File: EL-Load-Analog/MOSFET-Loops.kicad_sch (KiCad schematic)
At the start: 102 parts, among them J2 SWEB8094AU-SW, J5 SWEB8094AU-RT, J7 Conn_01x02_Socket, Q201 2N7002, Q202 2N7002, Q203 IRFP250M, Q204 IRFP250M, Q205 2N7002, Q206 2N7002, Q207 IRFP250M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

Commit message: Working on #4,#2 fixed #8,#22
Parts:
- C213, C214, C227, C228: value 470p -> 1n; Part Name C_470.0pF_0805_20% -> C_1.0nF_0805_20%
- R203, R205, R223, R225: value 100k -> 22k; Part Name R_100.0kΩ_0805_1% -> R_22.0kΩ_0805_1%
- R221, R222: value 10k -> 0; Part Name R_10.0kΩ_0805_1% -> R_0.0Ω_0805_1%
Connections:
- net GND: no longer R211.2, R213.2, R231.2, R233.2
- new net GCOM: R211.2, R213.2, R231.2, R233.2
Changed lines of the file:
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@@
     )
   )
+  (global_label "GCOM" (shape input) (at 201.93 135.89 180) (fields_autoplaced)
+    (effects (font (size 1.27 1.27)) (justify right))
+    (property "Intersheetrefs" "${INTERSHEET_REFS}" (at 193.7023 135.89 0)
+      (effects (font (size 1.27 1.27)) (justify right) hide)
+    )
+  )
   (global_label "LoadPlus" (shape input) (at 132.08 92.71 0) (fields_autoplaced)
     (effects (font (size 1.27 1.27)) (justify left))
@@
     )
   )
+  (global_label "GCOM" (shape input) (at 66.04 60.96 180) (fields_autoplaced)
+    (effects (font (size 1.27 1.27)) (justify right))
+    (property "Intersheetrefs" "${INTERSHEET_REFS}" (at 57.8123 60.96 0)
+      (effects (font (size 1.27 1.27)) (justify right) hide)
+    )
+  )
   (global_label "LoadPlus" (shape input) (at 267.97 17.78 0) (fields_autoplaced)
     (effects (font (size 1.27 1.27)) (justify left))
@@
     )
   )
+  (global_label "GCOM" (shape input) (at 66.04 135.89 180) (fields_autoplaced)
+    (effects (font (size 1.27 1.27)) (justify right))
+    (property "Intersheetrefs" "${INTERSHEET_REFS}" (at 57.8123 135.89 0)
+      (effects (font (size 1.27 1.27)) (justify right) hide)
+    )
+  )
   (global_label "LoadPlus" (shape input) (at 132.08 17.78 0) (fields_autoplaced)
     (effects (font (size 1.27 1.27)) (justify left))
@@
     )
   )
+  (global_label "GCOM" (shape input) (at 201.93 60.96 180) (fields_autoplaced)
+    (effects (font (size 1.27 1.27)) (justify right))
+    (property "Intersheetrefs" "${INTERSHEET_REFS}" (at 193.7023 60.96 0)
+      (effects (font (size 1.27 1.27)) (justify right) hide)
+    )
+  )
   (global_label "LoadPlus" (shape output) (at 92.71 179.07 0) (fields_autoplaced)
     (effects (font (size 1.27 1.27)) (justify left))
@@
     )
   )
-  (symbol (lib_id "power:GND") (at 66.04 135.89 0) (unit 1)
-    (in_bom yes) (on_board yes) (dnp no) (fields_autoplaced)
-    (property "Reference" "#PWR0218" (at 66.04 142.24 0)
-      (effects (font (size 1.27 1.27)) hide)
-    )
-    (property "Value" "GND" (at 66.04 140.97 0)
-      (effects (font (size 1.27 1.27)) hide)
-    )
-    (property "Footprint" "" (at 66.04 135.89 0)
-      (effects (font (size 1.27 1.27)) hide)
-    )
-    (property "Datasheet" "" (at 66.04 135.89 0)
-      (effects (font (size 1.27 1.27)) hide)
-    )
-    (pin "1")
-    (instances
-      (project "EL-Load-Analog"
-        (path "/51d9228f-95b8-4f0d-bdba-83c3975c517c/8af1df1b-1025-4aef-94e0-10ff3284a07d"
-          (reference "#PWR0218") (unit 1)
-        )
-      )
-    )
-  )
   (symbol (lib_id "Amplifier_Operational:LM318H") (at 185.42 29.21 0) (unit 1)
     (in_bom yes) (on_board yes) (dnp no) (fields_autoplaced)
@@
       (effects (font (size 1.27 1.27)))
     )
-    (property "Value" "470p" (at 191.7763 116.84 90)
+    (property "Value" "1n" (at 191.7763 116.84 90)
       (effects (font (size 1.27 1.27)))
     )
@@
       (effects (font (size 1.27 1.27)) hide)
     )
-    (property "Part Name" "C_470.0pF_0805_20%" (at 191.77 120.65 0)
+    (property "Part Name" "C_1.0nF_0805_20%" (at 191.77 120.65 0)
       (effects (font (size 1.27 1.27)) hide)
     )
@@
       (effects (font (size 1.27 1.27)))
     )
-    (property "Value" "470p" (at 55.8863 116.84 90)
+    (property "Value" "1n" (at 55.8863 116.84 90)
       (effects (font (size 1.27 1.27)))
     )
@@
       (effects (font (size 1.27 1.27)) hide)
     )
-    (property "Part Name" "C_470.0pF_0805_20%" (at 55.88 120.65 0)
+    (property "Part Name" "C_1.0nF_0805_20%" (at 55.88 120.65 0)
       (effects (font (size 1.27 1.27)) hide)
     )
@@
       (effects (font (size 1.27 1.27)))
     )
-    (property "Value" "470p" (at 55.8863 41.91 90)
+    (property "Value" "1n" (at 55.8863 41.91 90)
       (effects (font (size 1.27 1.27)))
     )
@@
       (effects (font (size 1.27 1.27)) hide)
     )
-    (property "Part Name" "C_470.0pF_0805_20%" (at 55.88 45.72 0)
+    (property "Part Name" "C_1.0nF_0805_20%" (at 55.88 45.72 0)
       (effects (font (size 1.27 1.27)) hide)
     )
@@
       (effects (font (size 1.27 1.27)))
     )
-    (property "Value" "100k" (at 175.26 138.43 90)
+    (property "Value" "22k" (at 175.26 138.43 90)
       (effects (font (size 1.27 1.27)))
     )
@@
       (effects (font (size 1.27 1.27)) hide)
     )
-    (property "Part Name" "R_100.0kΩ_0805_1%" (at 172.72 138.43 0)
+    (property "Part Name" "R_22.0kΩ_0805_1%" (at 172.72 138.43 0)
       (effects (font (size 1.27 1.27)) hide)
     )
@@
       (effects (font (size 1.27 1.27)))
     )
-    (property "Value" "100k" (at 39.37 63.5 90)
+    (property "Value" "22k" (at 39.37 63.5 90)
       (effects (font (size 1.27 1.27)))
     )
@@
       (effects (font (size 1.27 1.27)) hide)
     )
-    (property "Part Name" "R_100.0kΩ_0805_1%" (at 36.83 63.5 0)
+    (property "Part Name" "R_22.0kΩ_0805_1%" (at 36.83 63.5 0)
       (effects (font (size 1.27 1.27)) hide)
     )
@@
       (effects (font (size 1.27 1.27)))
     )
-    (property "Value" "100k" (at 39.37 138.43 90)
+    (property "Value" "22k" (at 39.37 138.43 90)
       (effects (font (size 1.27 1.27)))
     )
@@
       (effects (font (size 1.27 1.27)) hide)
     )
-    (property "Part Name" "R_100.0kΩ_0805_1%" (at 36.83 138.43 0)
+    (property "Part Name" "R_22.0kΩ_0805_1%" (at 36.83 138.43 0)
       (effects (font (size 1.27 1.27)) hide)
     )
@@
     )
   )
-  (symbol (lib_id "power:GND") (at 66.04 60.96 0) (unit 1)
-    (in_bom yes) (on_board yes) (dnp no) (fields_autoplaced)
-    (property "Reference" "#PWR0217" (at 66.04 67.31 0)
-      (effects (font (size 1.27 1.27)) hide)
-    )
-    (property "Value" "GND" (at 66.04 66.04 0)
-      (effects (font (size 1.27 1.27)) hide)
-    )
-    (property "Footprint" "" (at 66.04 60.96 0)
-      (effects (font (size 1.27 1.27)) hide)
-    )
-    (property "Datasheet" "" (at 66.04 60.96 0)
-      (effects (font (size 1.27 1.27)) hide)
-    )
-    (pin "1")
-    (instances
-      (project "EL-Load-Analog"
-        (path "/51d9228f-95b8-4f0d-bdba-83c3975c517c/8af1df1b-1025-4aef-94e0-10ff3284a07d"
-          (reference "#PWR0217") (unit 1)
-        )
-      )
-    )
-  )
   (symbol (lib_id "power:-5V") (at 182.88 36.83 180) (unit 1)
     (in_bom yes) (on_board yes) (dnp no)
@@
       (effects (font (size 1.27 1.27)))
     )
-    (property "Value" "10k" (at 162.56 99.06 90)
+    (property "Value" "0" (at 162.56 99.06 90)
       (effects (font (size 1.27 1.27)))
     )
@@
       (effects (font (size 1.27 1.27)) hide)
     )
-    (property "Part Name" "R_10.0kΩ_0805_1%" (at 162.56 101.6 0)
+    (property "Part Name" "R_0.0Ω_0805_1%" (at 162.56 101.6 0)
       (effects (font (size 1.27 1.27)) hide)
     )
@@
     )
   )
-  (symbol (lib_id "power:GND") (at 201.93 135.89 0) (unit 1)
-    (in_bom yes) (on_board yes) (dnp no) (fields_autoplaced)
-    (property "Reference" "#PWR0245" (at 201.93 142.24 0)
-      (effects (font (size 1.27 1.27)) hide)
-    )
-    (property "Value" "GND" (at 201.93 140.97 0)
-      (effects (font (size 1.27 1.27)) hide)
-    )
-    (property "Footprint" "" (at 201.93 135.89 0)
-      (effects (font (size 1.27 1.27)) hide)
-    )
-    (property "Datasheet" "" (at 201.93 135.89 0)
-      (effects (font (size 1.27 1.27)) hide)
-    )
-    (pin "1")
-    (instances
-      (project "EL-Load-Analog"
-        (path "/51d9228f-95b8-4f0d-bdba-83c3975c517c/8af1df1b-1025-4aef-94e0-10ff3284a07d"
-          (reference "#PWR0245") (unit 1)
-        )
-      )
-    )
-  )
   (symbol (lib_id "Device:R") (at 267.97 72.39 0) (unit 1)
     (in_bom yes) (on_board yes) (dnp no) (fields_autoplaced)
@@
     )
   )
-  (symbol (lib_id "power:GND") (at 201.93 60.96 0) (unit 1)
-    (in_bom yes) (on_board yes) (dnp no) (fields_autoplaced)
-    (property "Reference" "#PWR0244" (at 201.93 67.31 0)
-      (effects (font (size 1.27 1.27)) hide)
-    )
-    (property "Value" "GND" (at 201.93 66.04 0)
-      (effects (font (size 1.27 1.27)) hide)
-    )
-    (property "Footprint" "" (at 201.93 60.96 0)
-      (effects (font (size 1.27 1.27)) hide)
-    )
-    (property "Datasheet" "" (at 201.93 60.96 0)
-      (effects (font (size 1.27 1.27)) hide)
-    )
-    (pin "1")
-    (instances
-      (project "EL-Load-Analog"
-        (path "/51d9228f-95b8-4f0d-bdba-83c3975c517c/8af1df1b-1025-4aef-94e0-10ff3284a07d"
-          (reference "#PWR0244") (unit 1)
-        )
-      )
-    )
-  )
   (symbol (lib_id "Device:R_Small") (at 204.47 29.21 90) (unit 1)
     (in_bom yes) (on_board yes) (dnp no)
@@
       (effects (font (size 1.27 1.27)))
     )
-    (property "Value" "10k" (at 162.56 24.13 90)
+    (property "Value" "0" (at 162.56 24.13 90)
       (effects (font (size 1.27 1.27)))
     )
@@
       (effects (font (size 1.27 1.27)) hide)
     )
-    (property "Part Name" "R_10.0kΩ_0805_1%" (at 162.56 26.67 0)
+    (property "Part Name" "R_0.0Ω_0805_1%" (at 162.56 26.67 0)
       (effects (font (size 1.27 1.27)) hide)
     )
@@
       (effects (font (size 1.27 1.27)))
     )
-    (property "Value" "100k" (at 175.26 63.5 90)
+    (property "Value" "22k" (at 175.26 63.5 90)
       (effects (font (size 1.27 1.27)))
     )
@@
       (effects (font (size 1.27 1.27)) hide)
     )
-    (property "Part Name" "R_100.0kΩ_0805_1%" (at 172.72 63.5 0)
+    (property "Part Name" "R_22.0kΩ_0805_1%" (at 172.72 63.5 0)
       (effects (font (size 1.27 1.27)) hide)
     )
@@
       (effects (font (size 1.27 1.27)))
     )
-    (property "Value" "470p" (at 191.7763 41.91 90)
+    (property "Value" "1n" (at 191.7763 41.91 90)
       (effects (font (size 1.27 1.27)))
     )
@@
       (effects (font (size 1.27 1.27)) hide)
     )
-    (property "Part Name" "C_470.0pF_0805_20%" (at 191.77 45.72 0)
+    (property "Part Name" "C_1.0nF_0805_20%" (at 191.77 45.72 0)
       (effects (font (size 1.27 1.27)) hide)
     )

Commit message: Added heatsink moutingholes, reverse polarity, moved snubbers.
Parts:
- added Q7: AOSP66923, Package_SO:SO-8_3.9x4.9mm_P1.27mm, symbol EL-Load:AOSP66923
- added R25: 0, Resistor_SMD:R_0805_2012Metric, symbol Device:R_Small
- added TP4: Imon3, TestPoint:TestPoint_Pad_1.0x1.0mm, symbol Connector:TestPoint_Flag
- added TP5: Imon1, TestPoint:TestPoint_Pad_1.0x1.0mm, symbol Connector:TestPoint_Flag
- added TP6: Imon4, TestPoint:TestPoint_Pad_1.0x1.0mm, symbol Connector:TestPoint_Flag
- added TP7: Imon2, TestPoint:TestPoint_Pad_1.0x1.0mm, symbol Connector:TestPoint_Flag
- D203: value 1.5KE100A smd variant -> 1.5KE100A (smd)
- R23: now not fitted; now left out of the parts list
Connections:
- net GND: now also R25.1
- net LoadMin: now also Q7.1 (S), Q7.2 (S), Q7.3 (S), R25.2; no longer J2.1 (Pin_1), NT202.2, R23.1
- net at R225.2, R226.1, R234.2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: now also TP6.1
- net at R205.2, R206.1, R214.2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: now also TP4.1
- net at R223.2, R224.1, R232.2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: now also TP7.1
- net LoadPlusUnfused: now reaches F1.1, J5.1 (Pin_1), NT201.2
- net at R203.2, R204.1, R212.2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: now also TP5.1
- new net: J2.1 (Pin_1), NT202.2, Q7.5 (D), Q7.6 (D), Q7.7 (D), Q7.8 (D), R23.1
- new net ReverseProt: Q7.4 (G)
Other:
- note added: "MOSFET Loop 2"
- moved on the sheet: D203, J7

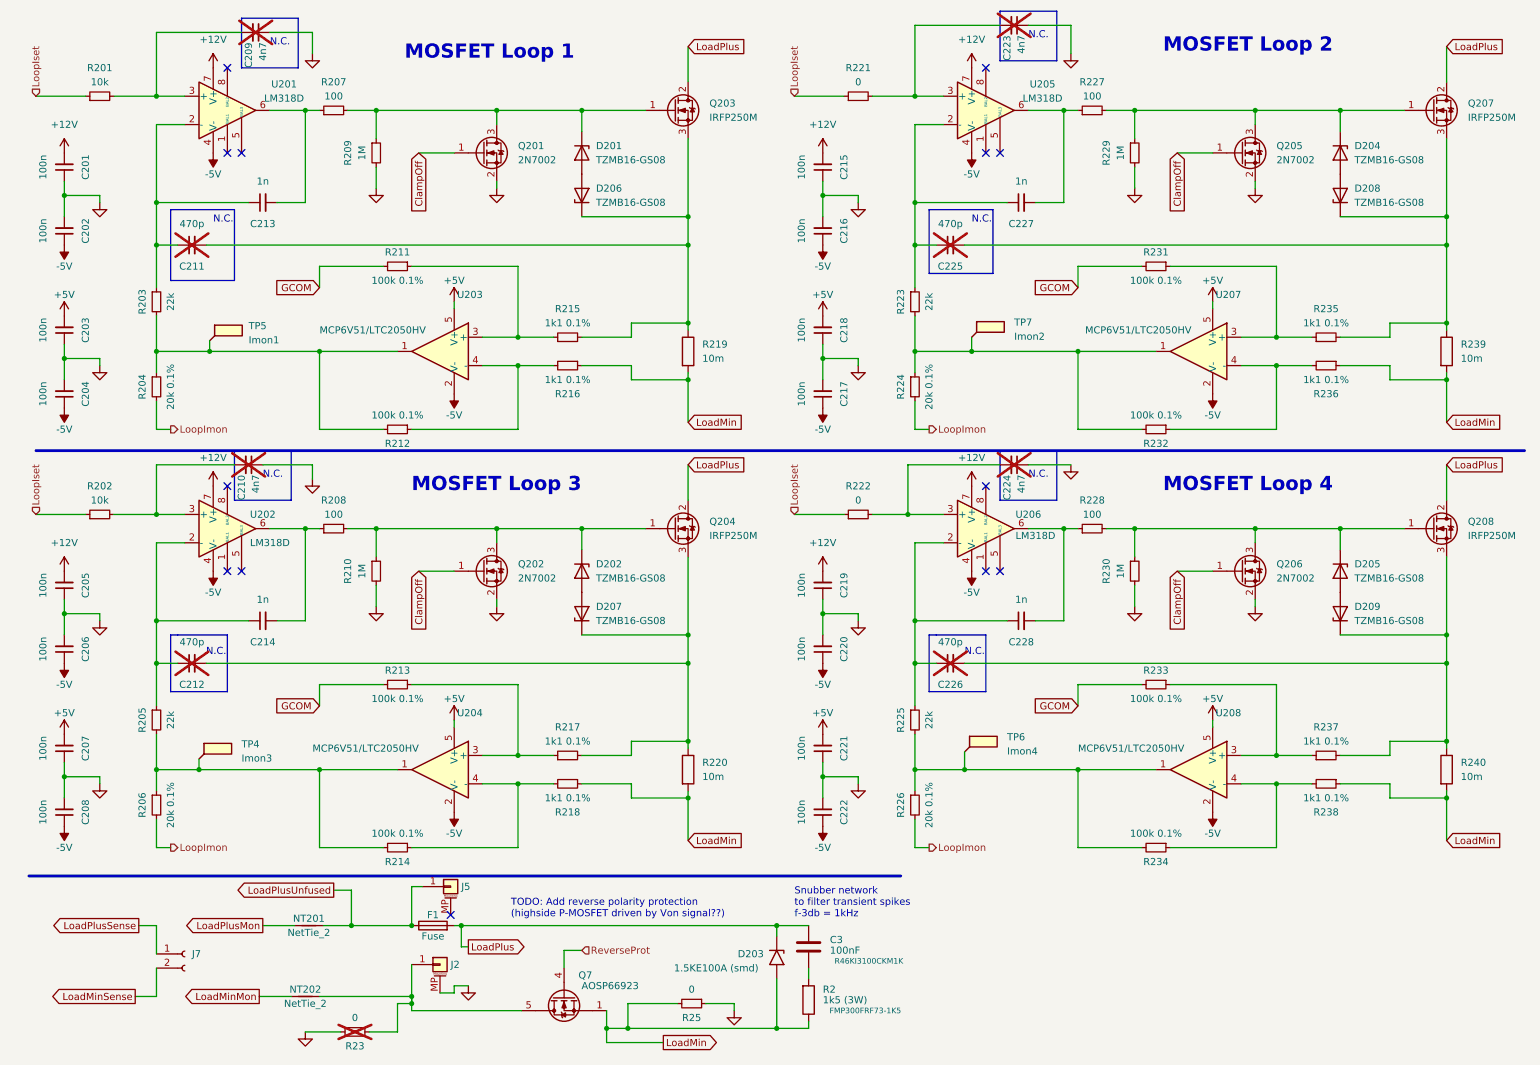
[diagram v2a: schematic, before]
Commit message: v4 Analog board design. Features reverse polarity, remote sense error and new clamping circuitry.
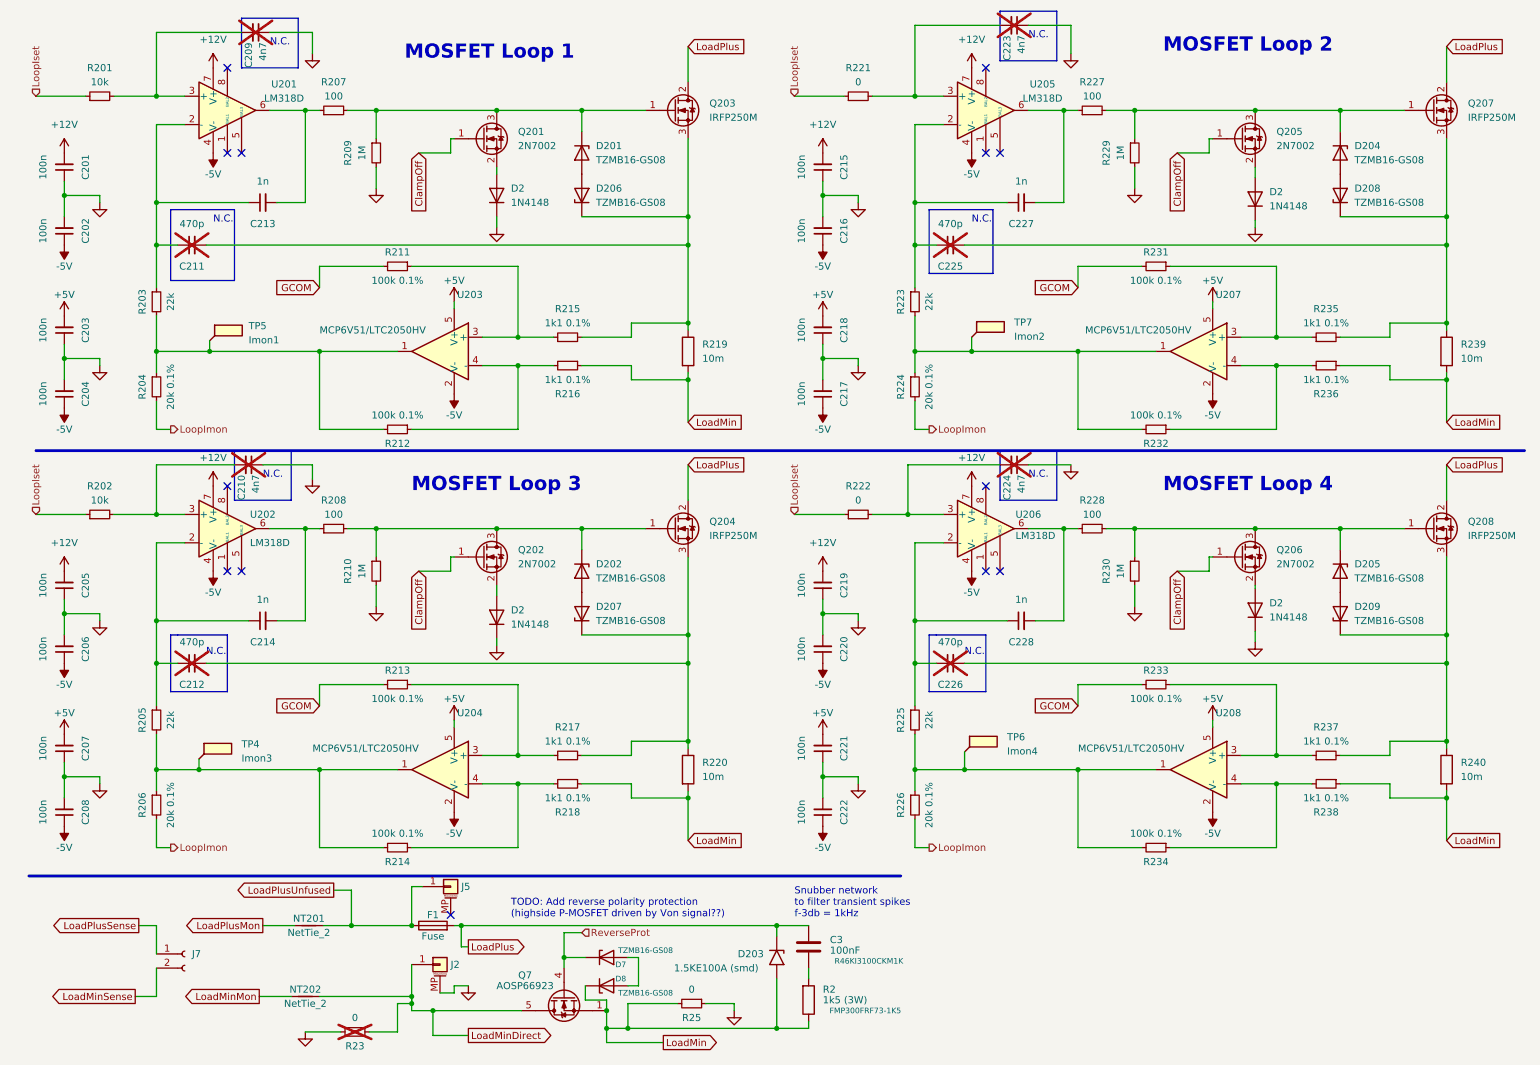
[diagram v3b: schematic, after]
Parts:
- added D2 (x4): 1N4148, Diode_SMD:D_MiniMELF, symbol Diode:1N4148
- added D7, D8: TZMB16-GS08, Diode_SMD:D_MiniMELF, symbol Device:D_Zener
- C201, C202, C203, C204, C205, C206, C207, C208, C215, C216, C217, C218, C219, C220, C221, C222: Part Name C_100.0nF_0805_20% -> C_100.0nF_50V_0805_10%_X7R
- F1: Part Name (none) -> FH_5x20_THT
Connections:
- net GND: now also D2.1 (K), D2.1 (K), D2.1 (K), D2.1 (K); no longer Q201.2 (S), Q202.2 (S), Q205.2 (S), Q206.2 (S)
- net LoadMin: now also D8.1 (K)
- net ReverseProt: now also D7.1 (K)
- net LoadMinDirect: now reaches J2.1 (Pin_1), NT202.2, Q7.5 (D), Q7.6 (D), Q7.7 (D), Q7.8 (D), R23.1
- new net: D2.2 (A), Q205.2 (S)
- new net: D2.2 (A), Q206.2 (S)
- new net: D2.2 (A), Q202.2 (S)
- new net: D2.2 (A), Q201.2 (S)
- new net: D7.2 (A), D8.2 (A)
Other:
- moved on the sheet: Q201, Q202, Q205, Q206
